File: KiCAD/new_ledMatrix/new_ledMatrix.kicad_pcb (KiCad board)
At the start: 2 copper layers, 72.6 x 39.1 mm, 62 parts

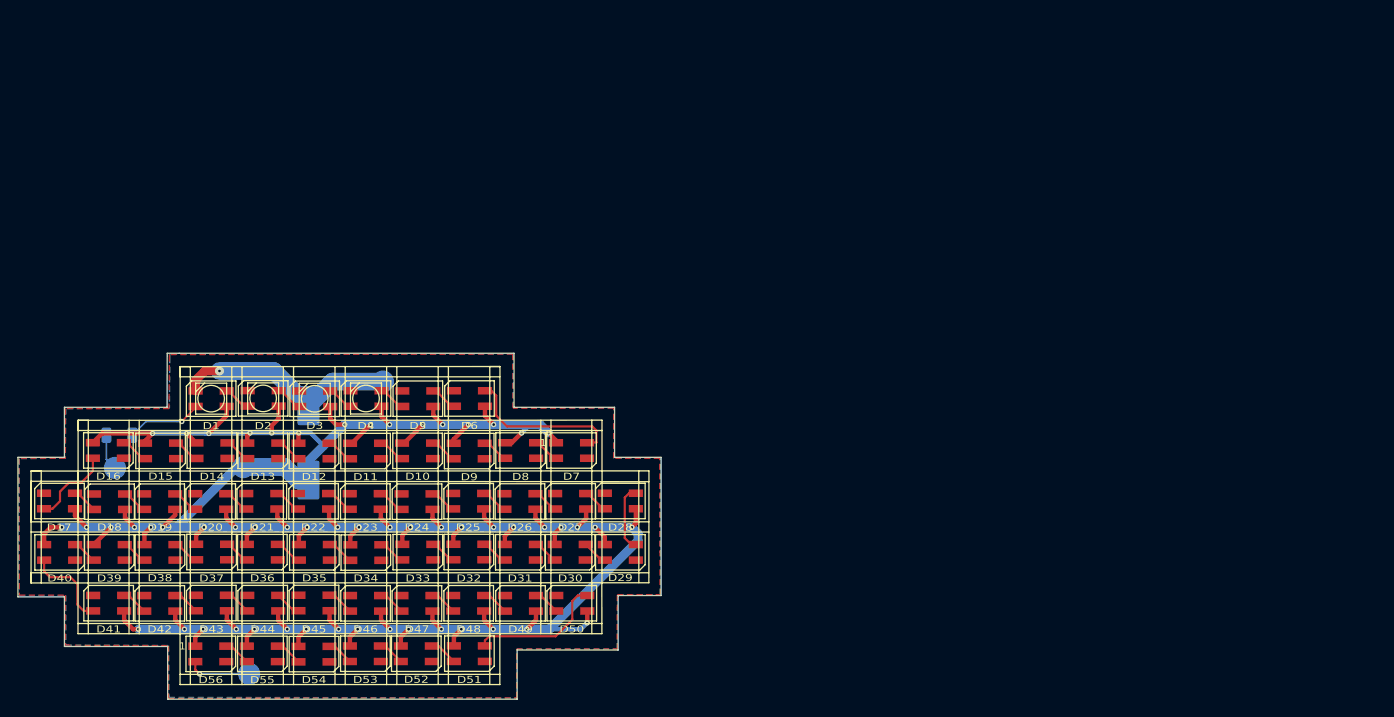
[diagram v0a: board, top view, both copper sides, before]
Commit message: Cleanup: keep single source STL/KiCad files; remove duplicates
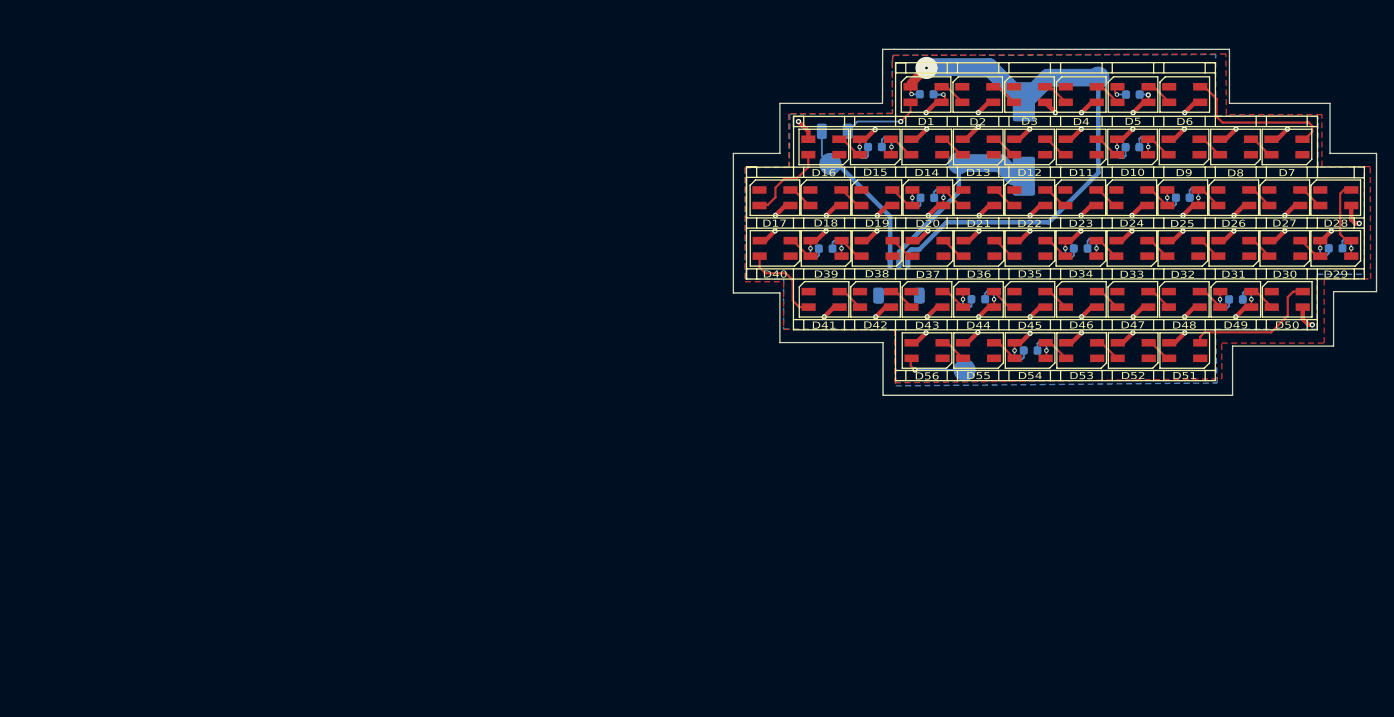
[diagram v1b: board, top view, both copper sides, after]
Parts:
- added JST_SH_SM03B: JST_SH_SM03B-SRSS-TB_1x03-1MP_P1.00mm_Horizontal, Connector_JST:JST_SH_SM03B-SRSS-TB_1x03-1MP_P1.00mm_Horizontal, B.Cu at (199.8, 50.5)
- added c10: 0.1uF, Capacitor_SMD:C_0603_1608Metric, B.Cu at (191.5, 47.0)
- added c11: 0.1uF, Capacitor_SMD:C_0603_1608Metric, B.Cu at (208.7, 52.8)
- added c12: 0.1uF, Capacitor_SMD:C_0603_1608Metric, B.Cu at (237.8, 52.8)
- added c13: 0.1uF, Capacitor_SMD:C_0603_1608Metric, B.Cu at (214.6, 58.5)
- added c2: 0.1uF, Capacitor_SMD:C_0603_1608Metric, B.Cu at (202.9, 29.6)
- added c3: 0.1uF, Capacitor_SMD:C_0603_1608Metric, B.Cu at (226.2, 29.6)
- added c4: 0.1uF, Capacitor_SMD:C_0603_1608Metric, B.Cu at (226.1, 35.6)
- added c5: 0.1uF, Capacitor_SMD:C_0603_1608Metric, B.Cu at (197.0, 35.6)
- added c6: 0.1uF, Capacitor_SMD:C_0603_1608Metric, B.Cu at (203.0, 41.3)
- added c7: 0.1uF, Capacitor_SMD:C_0603_1608Metric, B.Cu at (231.8, 41.3)
- added c8: 0.1uF, Capacitor_SMD:C_0603_1608Metric, B.Cu at (249.0, 47.0)
- added c9: 0.1uF, Capacitor_SMD:C_0603_1608Metric, B.Cu at (220.3, 47.0)
- C1: value 1000uF(10x10.5mm) -> 1000uF
- moved D19 87.9 mm to (197.3, 41.3)
- moved D38 87.9 mm to (197.3, 47.0)
- moved D20 87.9 mm to (203.0, 41.3)
- moved D21 87.9 mm to (208.8, 41.3)
- moved D39 87.9 mm to (191.5, 47.0)
- moved D52 87.9 mm to (226.2, 58.5)
- moved D36 87.9 mm to (208.8, 47.0)
- moved D18 87.8 mm to (191.5, 41.3)
- moved D37 87.8 mm to (203.0, 47.0)
- moved D22 87.8 mm to (214.5, 41.3)
- moved D56 87.8 mm to (202.9, 58.5)
- moved D55 87.8 mm to (208.7, 58.5)
- moved D53 87.8 mm to (220.4, 58.5)
- moved D54 87.8 mm to (214.6, 58.5)
- moved D47 87.8 mm to (226.2, 52.8)
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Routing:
- net +5V: track 349.0 -> 187.2 mm, vias 55 -> 68
- net GND: track 26.0 -> 101.8 mm, vias 1 -> 13
- net Net-(R1-Pad1): track 4.10 -> 18.4 mm
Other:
- board size 72.6 x 39.1 mm -> 72.6 x 39 mm
- board text added: "minecraft_compass led_matrix"
- board text removed: "minecraft_compass_led_matrix"

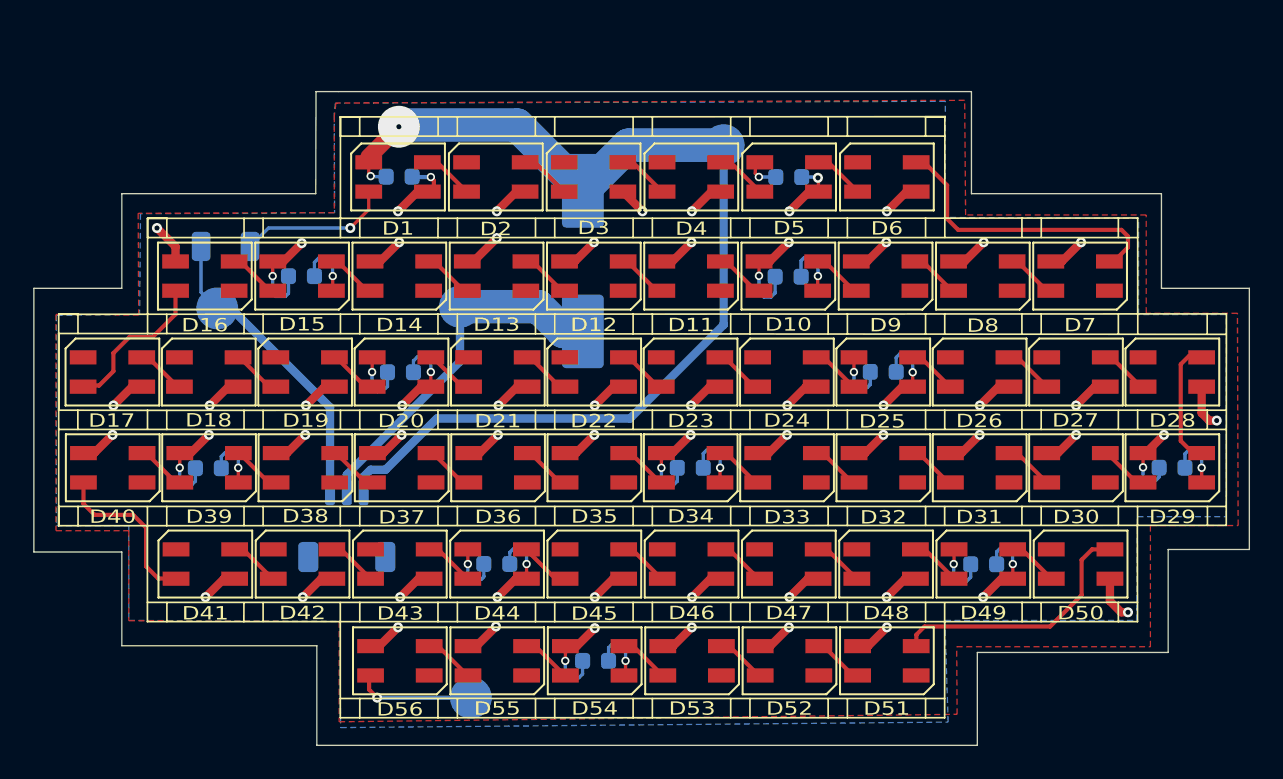
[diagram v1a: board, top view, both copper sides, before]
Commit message: upadted pcb to ver7
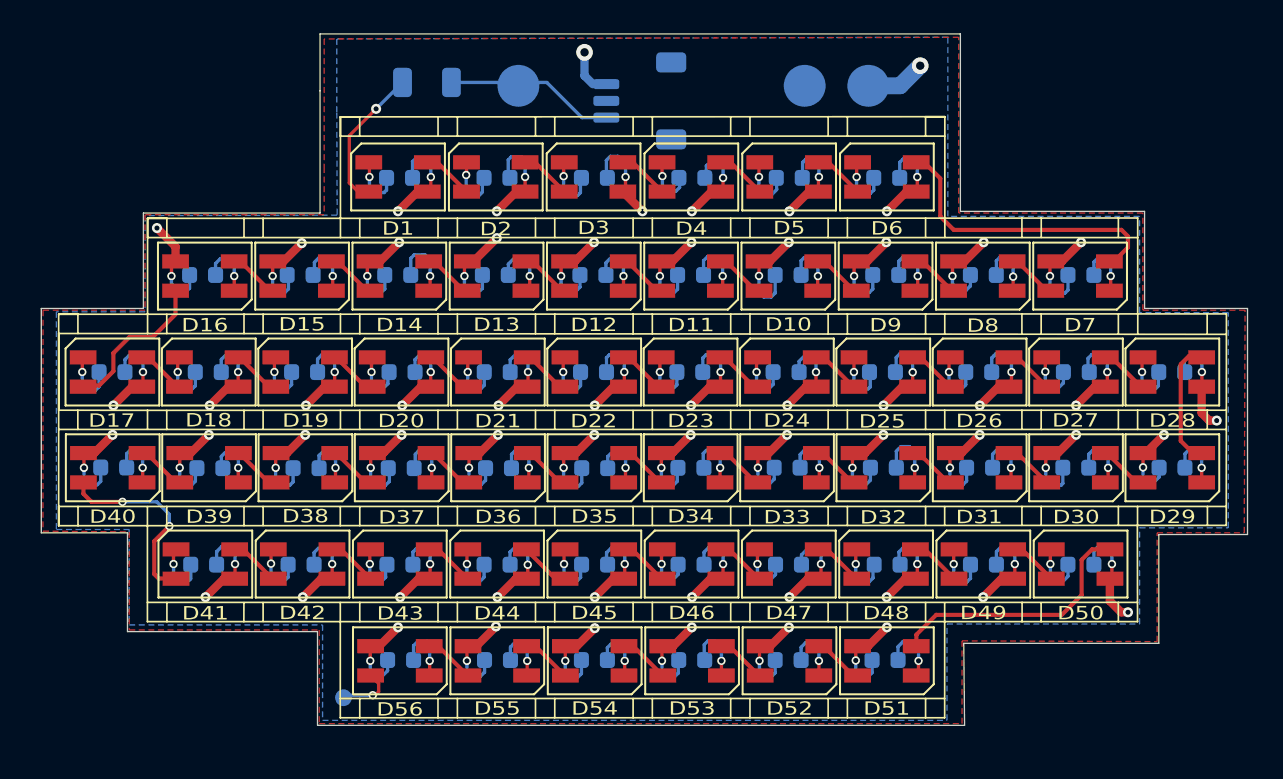
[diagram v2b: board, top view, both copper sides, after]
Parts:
- removed C1: 1000uF, Capacitor_SMD:CP_Elec_10x10.5
- removed JST_SH_SM03B: JST_SH_SM03B-SRSS-TB_1x03-1MP_P1.00mm_Horizontal, Connector_JST:JST_SH_SM03B-SRSS-TB_1x03-1MP_P1.00mm_Horizontal
- added G5D: JST_SH_SM03B-SRSS-TB_1x03-1MP_P1.00mm_Horizontal, Connector_JST:JST_SH_SM03B-SRSS-TB_1x03-1MP_P1.00mm_Horizontal, B.Cu at (217.2, 25.1)
- added c11: 0.1uF, Capacitor_SMD:C_0603_1608Metric, B.Cu at (220.3, 35.5)
- added c12: 0.1uF, Capacitor_SMD:C_0603_1608Metric, B.Cu at (214.5, 35.5)
- added c13: 0.1uF, Capacitor_SMD:C_0603_1608Metric, B.Cu at (208.6, 35.5)
- added c14: 0.1uF, Capacitor_SMD:C_0603_1608Metric, B.Cu at (202.8, 35.5)
- added c16: 0.1uF, Capacitor_SMD:C_0603_1608Metric, B.Cu at (191.1, 35.5)
- added c17: 0.1uF, Capacitor_SMD:C_0603_1608Metric, B.Cu at (185.7, 41.3)
- added c18: 0.1uF, Capacitor_SMD:C_0603_1608Metric, B.Cu at (191.5, 41.3)
- added c19: 0.1uF, Capacitor_SMD:C_0603_1608Metric, B.Cu at (197.2, 41.3)
- added c2: 0.1uF, Capacitor_SMD:C_0603_1608Metric, B.Cu at (208.7, 29.7)
- added c21: 0.1uF, Capacitor_SMD:C_0603_1608Metric, B.Cu at (208.7, 41.3)
- added c22: 0.1uF, Capacitor_SMD:C_0603_1608Metric, B.Cu at (214.5, 41.3)
- added c23: 0.1uF, Capacitor_SMD:C_0603_1608Metric, B.Cu at (220.2, 41.3)
- added c24: 0.1uF, Capacitor_SMD:C_0603_1608Metric, B.Cu at (226.0, 41.3)
- added c26: 0.1uF, Capacitor_SMD:C_0603_1608Metric, B.Cu at (237.5, 41.3)
- added c28: 0.1uF, Capacitor_SMD:C_0603_1608Metric, B.Cu at (249.0, 41.3)
- added c3: 0.1uF, Capacitor_SMD:C_0603_1608Metric, B.Cu at (214.5, 29.7)
- added c30: 0.1uF, Capacitor_SMD:C_0603_1608Metric, B.Cu at (243.3, 47.0)
- added c31: 0.1uF, Capacitor_SMD:C_0603_1608Metric, B.Cu at (237.5, 47.0)
- added c32: 0.1uF, Capacitor_SMD:C_0603_1608Metric, B.Cu at (231.8, 47.0)
- added c33: 0.1uF, Capacitor_SMD:C_0603_1608Metric, B.Cu at (226.1, 47.0)
- added c35: 0.1uF, Capacitor_SMD:C_0603_1608Metric, B.Cu at (214.6, 47.0)
- added c36: 0.1uF, Capacitor_SMD:C_0603_1608Metric, B.Cu at (208.8, 47.0)
- added c37: 0.1uF, Capacitor_SMD:C_0603_1608Metric, B.Cu at (203.0, 47.0)
- added c38: 0.1uF, Capacitor_SMD:C_0603_1608Metric, B.Cu at (197.3, 47.0)
- added c4: 0.1uF, Capacitor_SMD:C_0603_1608Metric, B.Cu at (220.4, 29.7)
- added c40: 0.1uF, Capacitor_SMD:C_0603_1608Metric, B.Cu at (185.8, 47.0)
- added c41: 0.1uF, Capacitor_SMD:C_0603_1608Metric, B.Cu at (191.2, 52.8)
- added c42: 0.1uF, Capacitor_SMD:C_0603_1608Metric, B.Cu at (197.0, 52.8)
- added c43: 0.1uF, Capacitor_SMD:C_0603_1608Metric, B.Cu at (202.9, 52.8)
- added c45: 0.1uF, Capacitor_SMD:C_0603_1608Metric, B.Cu at (214.6, 52.8)
- added c46: 0.1uF, Capacitor_SMD:C_0603_1608Metric, B.Cu at (220.3, 52.8)
- added c47: 0.1uF, Capacitor_SMD:C_0603_1608Metric, B.Cu at (226.1, 52.8)
- added c48: 0.1uF, Capacitor_SMD:C_0603_1608Metric, B.Cu at (232.0, 52.8)
- added c5: 0.1uF, Capacitor_SMD:C_0603_1608Metric, B.Cu at (226.2, 29.7)
- added c50: 0.1uF, Capacitor_SMD:C_0603_1608Metric, B.Cu at (243.6, 52.8)
- added c51: 0.1uF, Capacitor_SMD:C_0603_1608Metric, B.Cu at (231.9, 58.5)
- added c52: 0.1uF, Capacitor_SMD:C_0603_1608Metric, B.Cu at (226.1, 58.5)
- added c54: 0.1uF, Capacitor_SMD:C_0603_1608Metric, B.Cu at (214.5, 58.5)
- added c55: 0.1uF, Capacitor_SMD:C_0603_1608Metric, B.Cu at (208.8, 58.5)
- added c56: 0.1uF, Capacitor_SMD:C_0603_1608Metric, B.Cu at (203.0, 58.5)
- added c6: 0.1uF, Capacitor_SMD:C_0603_1608Metric, B.Cu at (232.0, 29.7)
- added c7: 0.1uF, Capacitor_SMD:C_0603_1608Metric, B.Cu at (243.6, 35.5)
- added c8: 0.1uF, Capacitor_SMD:C_0603_1608Metric, B.Cu at (237.8, 35.5)
- added c9: 0.1uF, Capacitor_SMD:C_0603_1608Metric, B.Cu at (231.9, 35.5)
- moved TP1 24.5 mm to (227.1, 24.2)
- moved TP3 22.4 mm to (210.0, 24.2)
- moved c27 20.8 mm to (243.3, 41.3)
- moved R1 15.5 mm to (204.5, 24.0), turned to 180 degrees
- moved TP2 9.34 mm to (230.9, 24.2)
- moved TP4 7.61 mm to (199.6, 60.8)
- moved c53 5.74 mm to (220.3, 58.5), turned to 0 degrees
- moved c15 0.10 mm to (197.0, 35.5), turned to 0 degrees
- moved c10 0.10 mm to (226.1, 35.5)
- moved c20 0.10 mm to (203.1, 41.3), turned to 180 degrees
- moved c39 0.09 mm to (191.6, 47.0)
- moved c1 0.08 mm to (202.9, 29.7)
- turned c25 to 180 degrees
- turned c44 to 180 degrees
- turned c49 to 180 degrees
- renumbered c2 to c1, c4 to c10, c5 to c15, c6 to c20, c7 to c25, c3 to c27, c8 to c29, c9 to c34, c10 to c39, c11 to c44, c12 to c49, c13 to c53
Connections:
- c15 pad 1: GND -> +5V
- c15 pad 2: +5V -> GND
- c20 pad 1: GND -> +5V
- c20 pad 2: +5V -> GND
- c25 pad 1: GND -> +5V
- c25 pad 2: +5V -> GND
- c44 pad 1: GND -> +5V
- c44 pad 2: +5V -> GND
- c49 pad 1: GND -> +5V
- c49 pad 2: +5V -> GND
- c53 pad 1: GND -> +5V
- c53 pad 2: +5V -> GND
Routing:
- net +5V: track 187.2 -> 330.5 mm, vias 68 -> 112
- net GND: track 101.8 -> 216.8 mm, vias 13 -> 58
- net Net-(R1-Pad1): track 18.4 -> 9.32 mm
- net Net-(D56-DOUT): track 7.18 -> 3.42 mm
- net Net-(D40-DOUT): track 10.0 -> 11.7 mm, vias 0 -> 2
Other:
- board size 72.6 x 39 mm -> 72.1 x 41.3 mm
- board text added: "minecraft_compass"
- board text removed: "minecraft_compass led_matrix"

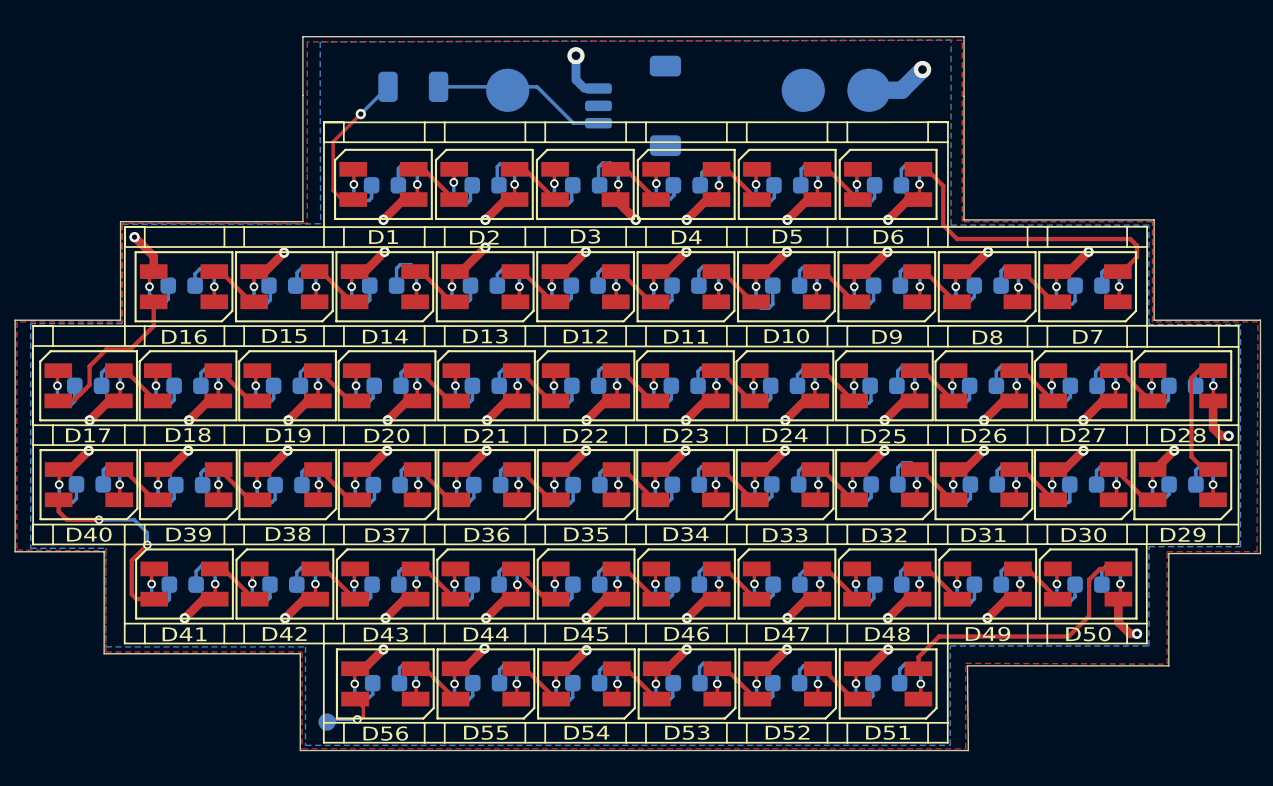
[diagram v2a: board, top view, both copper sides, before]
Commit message: pcb hole placement fixed, also added it in freecad model view
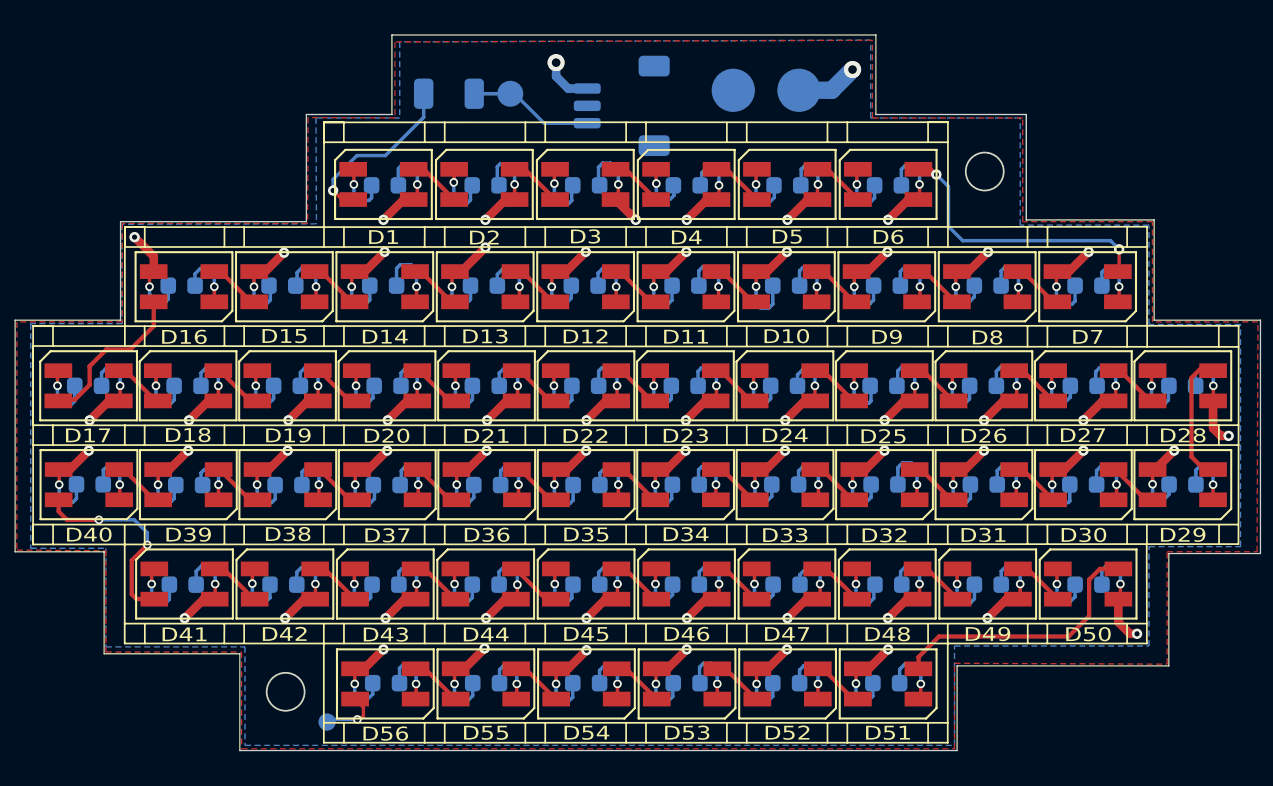
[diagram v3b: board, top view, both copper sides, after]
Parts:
- moved TP2 4.05 mm to (226.8, 24.2)
- moved TP1 4.05 mm to (223.1, 24.2)
- moved R1 2.10 mm to (206.6, 24.4)
- moved G5D 0.65 mm to (216.6, 25.1)
- moved TP3 0.25 mm to (210.2, 24.4)
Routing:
- net Net-(R1-Pad1): track 9.32 -> 7.89 mm
- net Net-(D1-DIN): track 8.69 -> 10.1 mm
- net Net-(D6-DOUT): track 18.0 -> 17.0 mm, vias 0 -> 2
- net GND: track 216.8 -> 217.7 mm
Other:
- board size 72.1 x 41.3 mm -> 72.1 x 41.4 mm
